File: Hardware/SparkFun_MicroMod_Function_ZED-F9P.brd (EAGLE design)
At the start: 38 x 65 mm, 112 parts, among them J1 USB Female Type C Connector, J10 U.FL, J11 455-1750-1-ND, J15 QWIIC_VERT, J16 QWIIC_RA, J18 Bus Selection, J2 MICROMOD_STANDARD, J3 Bus Selection, Q1 DMP21D0UT, U1 SN74LVC1G66DRYR, U10 SN74AUP1T04DCK, U11 SN74AUP1T04DCK, U2 3.3V, U3 EEPROM, U4 74LVC4066D_QUAD_BILATERAL_SWI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, U5 74LVC4066D_QUAD_BILATERAL_SWI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, U6 OPA344, U7 74LVC541ABQ, U8 U-BLOX_ZED-F9P, U9 FIN1017MXSOIC-8

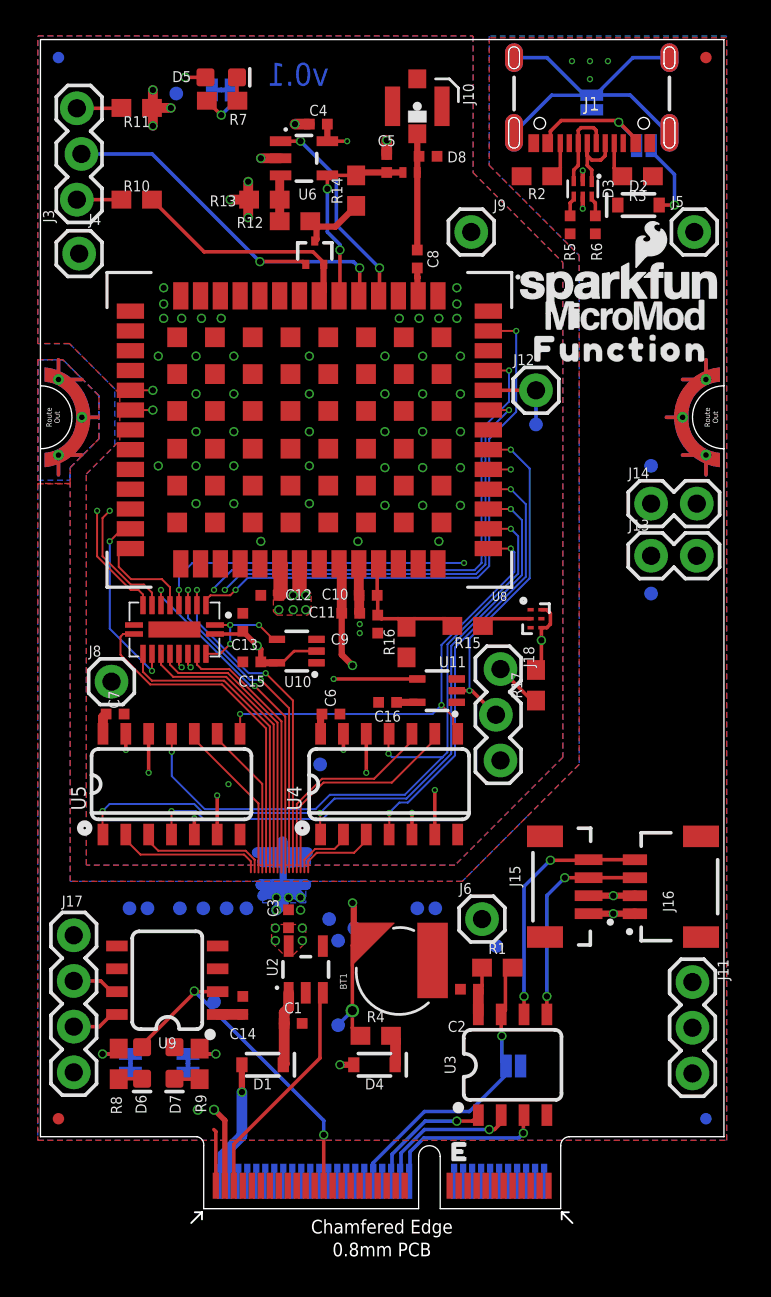
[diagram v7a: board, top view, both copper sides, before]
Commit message: End of day commit.
Rearchitected plane placement based on rank.
Began routing digital signals to end points.
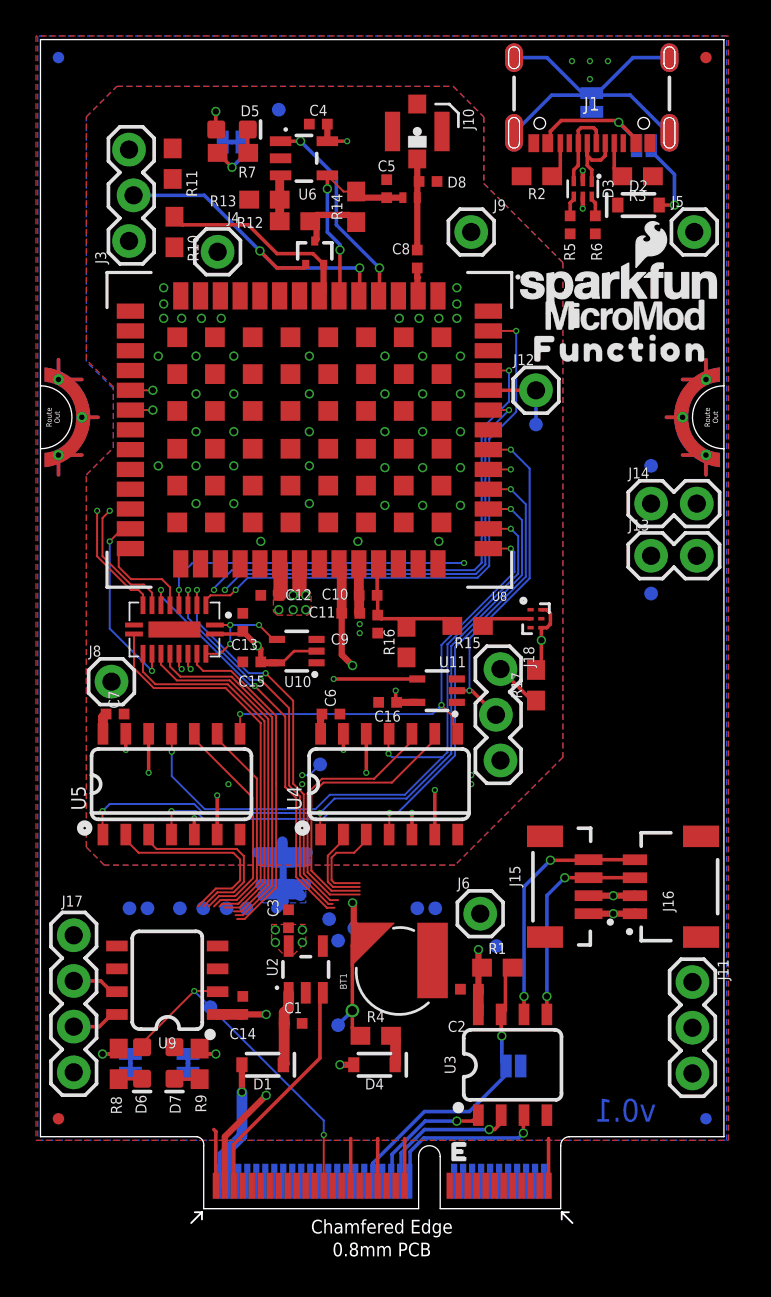
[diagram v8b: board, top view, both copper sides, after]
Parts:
- JP3: value JUMPER-SMT_2_NO_SILK -> JUMPER-SMT_2_NC_TRACE_SILK; device SparkFun-Jumpers:SMT-JUMPER_2_NO_SILK -> SparkFun-Jumpers:SMT-JUMPER_2_NC_TRACE_SILK
- moved J4 7.70 mm to (9.90, 53.2)
- moved TP4 5.77 mm to (13.3, 61.1)
- moved J3 3.70 mm to (5.10, 53.8)
- moved R11 3.69 mm to (7.40, 58.1), turned to 90 degrees
- moved JP4 2.96 mm to (10.7, 59.3)
- moved D5 2.96 mm to (10.7, 60.0)
- moved R7 2.96 mm to (10.8, 58.7)
- moved R10 2.77 mm to (7.50, 54.3), turned to 90 degrees
- moved C5 1.40 mm to (19.3, 56.7)
- moved D8 1.40 mm to (21.6, 57.1)
- moved J10 1.40 mm to (21.0, 59.9)
- moved L1 1.40 mm to (20.6, 56.2)
- moved R14 0.90 mm to (17.6, 55.7)
- moved TP9 0.36 mm to (9.50, 11.2)
- moved J6 0.32 mm to (24.5, 16.4)
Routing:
- net 3.3V: track 11.8 -> 44.2 mm, vias 4 -> 5
- net GND: track 12.6 -> 23.0 mm, vias 11 -> 6
- net GND_RF: track 18.0 -> 9.11 mm, vias 58 -> 49
- net V_USB: track 8.76 -> 14.4 mm
- net PPS: track 34.4 -> 38.1 mm
- net ZED_ANT_OFF: track 22.3 -> 18.9 mm
- net TX_READY: track 16.2 -> 19.6 mm
- net MM_COPI: track 9.19 -> 12.5 mm
- net RX2/RTCM: track 19.6 -> 22.9 mm
- net MM_CIPO: track 8.75 -> 12.0 mm
- net RTK_STAT: track 17.4 -> 20.7 mm
- net MM_RX: track 12.1 -> 15.2 mm
- net TX2/RTCM: track 16.5 -> 19.6 mm
- net EXTINT: track 19.2 -> 22.1 mm
- net MM_SCK: track 7.39 -> 10.3 mm
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- added copper zone on layer 15, net GND
- added copper zone on layer 2, net V_ZED
- removed copper zone on layer 15, net 3.3V
- removed copper zone on layer 15, net V_USB
